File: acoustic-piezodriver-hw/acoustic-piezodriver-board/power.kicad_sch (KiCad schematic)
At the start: 29 parts, among them J2 Conn_02x04_Odd_Even, U1 LM3478MM, U4 LM3478MM, U5 LM3478MM, U8 NCE6005AS

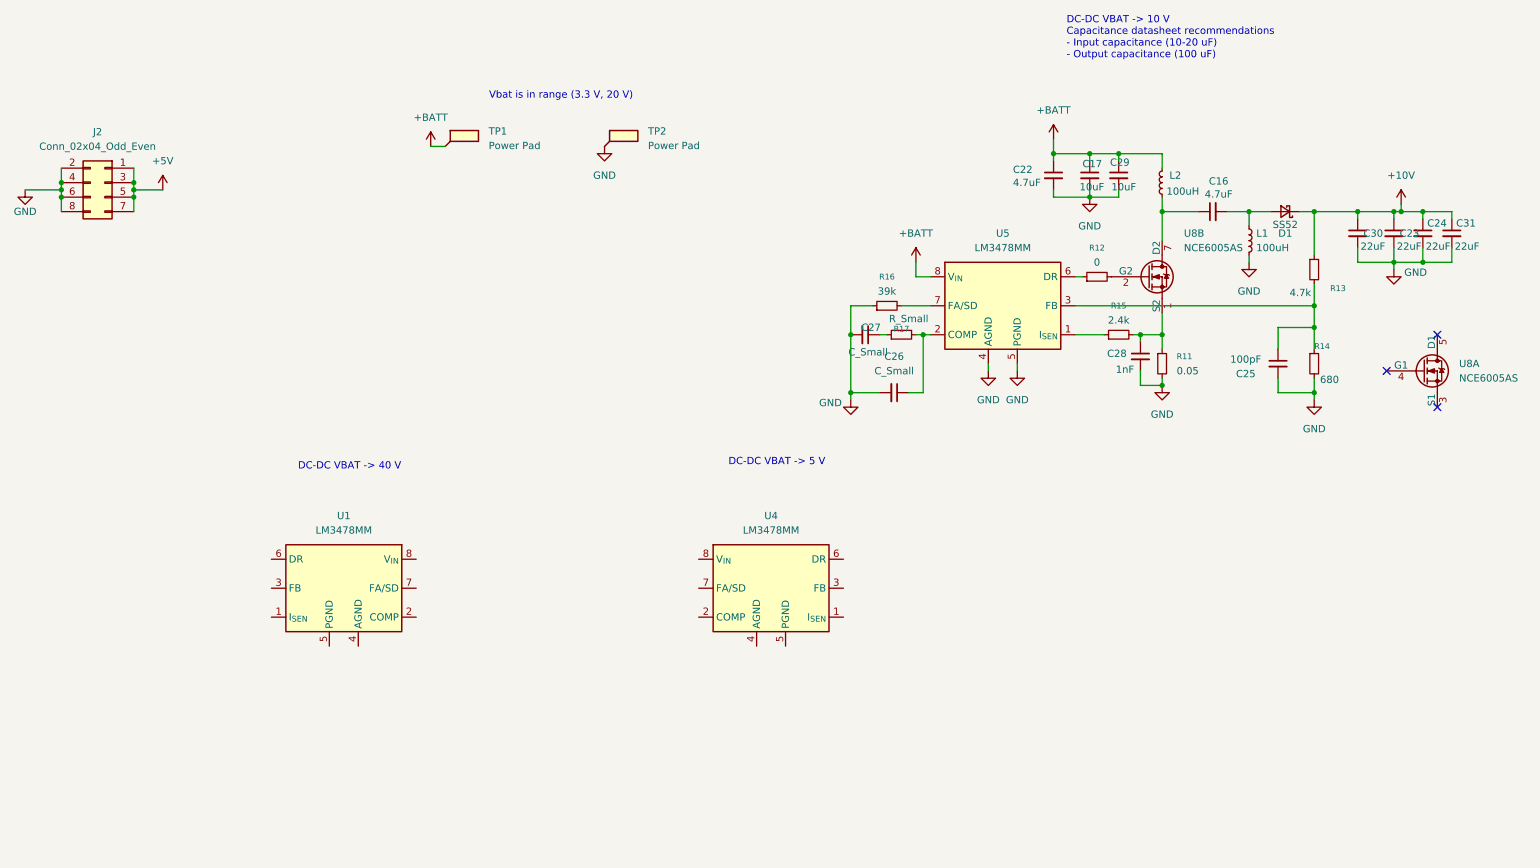
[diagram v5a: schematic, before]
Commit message: [piezodriver] Finished 2 sepic designs, starting boost design (warn) Make sure to max diode voltage difference
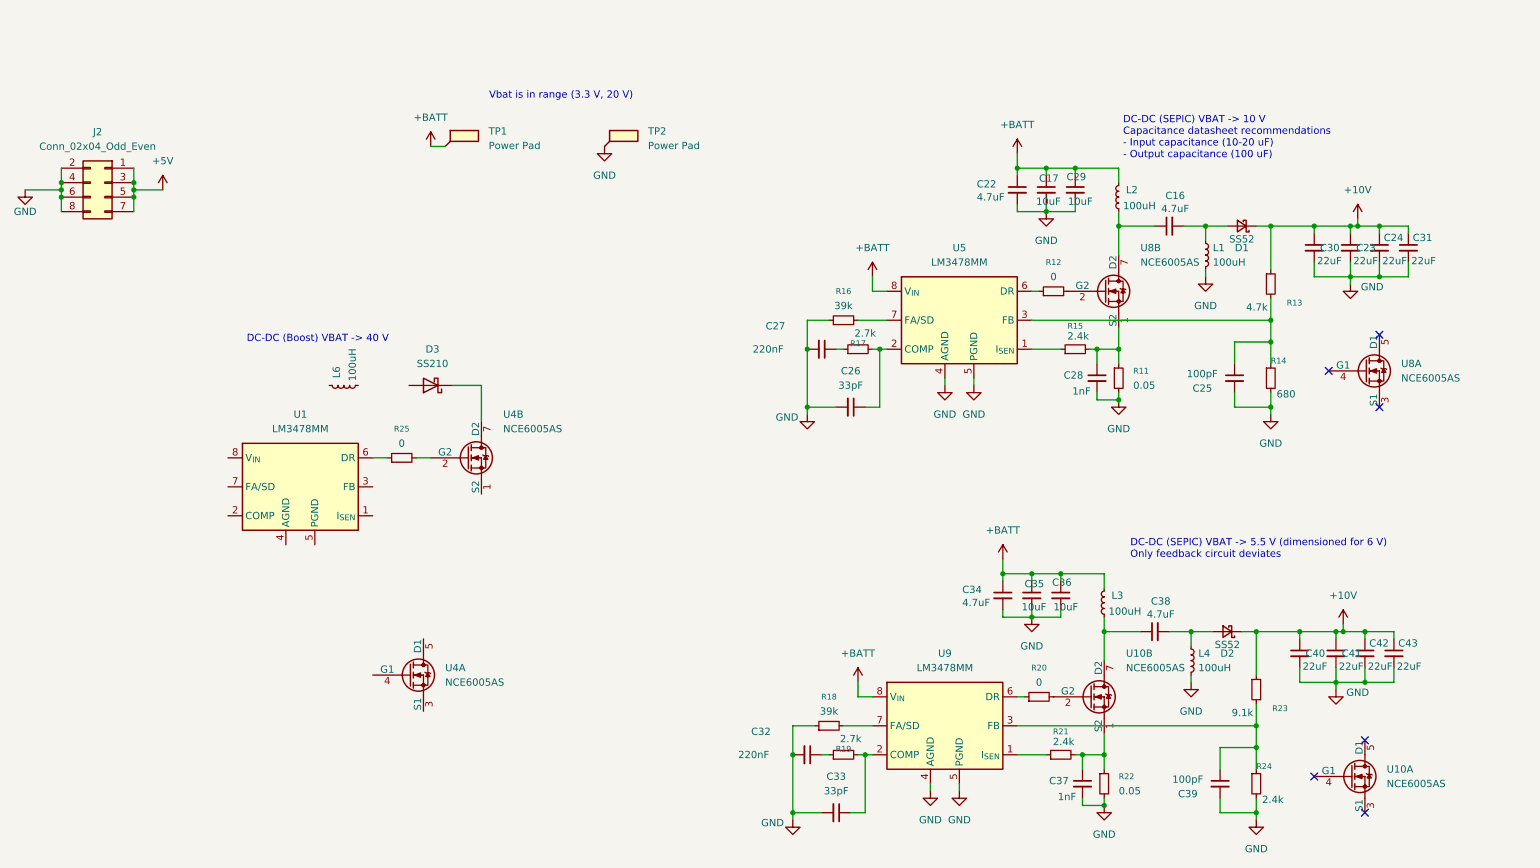
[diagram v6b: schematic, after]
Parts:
- removed U4: LM3478MM, Package_SO:VSSOP-8_3x3mm_P0.65mm, symbol Regulator_Controller:LM3478MM
- added C32: 220nF, Capacitor_SMD:C_0603_1608Metric, symbol Device:C_Small
- added C33: 33pF, Capacitor_SMD:C_0603_1608Metric, symbol Device:C_Small
- added C34, C38: 4.7uF, Capacitor_SMD:C_1206_3216Metric, symbol Device:C_Small
- added C35, C36: 10uF, Capacitor_SMD:C_0805_2012Metric, symbol Device:C_Small
- added C37: 1nF, Capacitor_SMD:C_0402_1005Metric, symbol Device:C_Small
- added C39: 100pF, Capacitor_SMD:C_0402_1005Metric, symbol Device:C_Small
- added C40, C41, C42, C43: 22uF, Capacitor_SMD:C_0805_2012Metric, symbol Device:C_Small
- added D2: SS52, Diode_SMD:D_SMA-SMB_Universal_Handsoldering, symbol Device:D_Schottky_Small
- added D3: SS210, Diode_SMD:D_SMA, symbol Diode:SS210
- added L3, L4, L6: 100uH, symbol Device:L_Small
- added R18: 39k, Resistor_SMD:R_0603_1608Metric, symbol Device:R_Small
- added R19: 2.7k, Resistor_SMD:R_0603_1608Metric, symbol Device:R_Small
- added R20, R25: 0, Resistor_SMD:R_0603_1608Metric_Pad0.98x0.95mm_HandSolder, symbol Device:R_Small
- added R21: 2.4k, Resistor_SMD:R_0805_2012Metric_Pad1.20x1.40mm_HandSolder, symbol Device:R_Small
- added R22: 0.05, Resistor_SMD:R_1206_3216Metric_Pad1.30x1.75mm_HandSolder, symbol Device:R_Small
- added R23: 9.1k, Resistor_SMD:R_0603_1608Metric, symbol Device:R_Small
- added R24: 2.4k, Resistor_SMD:R_0603_1608Metric, symbol Device:R_Small
- added U10, U4: NCE6005AS, symbol custom_mosfet:NCE6005AS
- added U9: LM3478MM, Package_SO:VSSOP-8_3x3mm_P0.65mm, symbol Regulator_Controller:LM3478MM
- C25: footprint (none) -> Capacitor_SMD:C_0402_1005Metric; LPN (none) -> C1546; MPN (none) -> 0402CG101J500NT
- C26: value C_Small -> 33pF; footprint (none) -> Capacitor_SMD:C_0603_1608Metric; LPN (none) -> C1663; MPN (none) -> CL10C330JB8NNNC
- C27: value C_Small -> 220nF; footprint (none) -> Capacitor_SMD:C_0603_1608Metric
- C28: footprint (none) -> Capacitor_SMD:C_0402_1005Metric; LPN (none) -> C1523; MPN (none) -> 0402B102K500NT
- R12: footprint (none) -> Resistor_SMD:R_0603_1608Metric_Pad0.98x0.95mm_HandSolder; LPN (none) -> C15402; MPN (none) -> 0603WAJ0000T5E
- R17: value R_Small -> 2.7k; footprint (none) -> Resistor_SMD:R_0603_1608Metric; LPN (none) -> C13167; MPN (none) -> 0603WAF2701T5E
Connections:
- net +10V: now also C40.1, C41.1, C42.1, C43.1, D2.1 (K), R23.1
- net +BATT: now also C34.1, C35.1, C36.1, L3.2, U9.8 (V_{IN})
- net GND: now also C32.2, C33.2, C34.2, C35.2, C36.2, C37.2, C39.2, C40.2, C41.2, C42.2, C43.2, L4.2, R18.1, R22.2, R24.2, U9.4 (AGND), U9.5 (PGND)
- net at U1.6 (DR): now also R25.1
- new net: U4.5 (D1), U4.6 (D1)
- new net: C38.1, L3.1, U10.7 (D2), U10.8 (D2)
- new net: C38.2, D2.2 (A), L4.1
- new net: R18.2, U9.7 (FA/SD)
- new net: C39.1, R23.2, R24.1, U9.3 (FB)
- new net: C37.1, R21.2, R22.1, U10.1 (S2)
- new net: C32.1, R19.1
- new net: C33.1, R19.2, U9.2 (COMP)
- new net: R25.2, U4.2 (G2)
- new net: D3.1 (K), U4.7 (D2), U4.8 (D2)
- new net: R20.1, U9.6 (DR)
- new net: R20.2, U10.2 (G2)
- new net: R21.1, U9.1 (I_{SEN})
- new net: U10.5 (D1), U10.6 (D1)
- no-connect marks 3 -> 6
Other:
- note added: "DC-DC (Boost) VBAT -> 40 V"
- note added: "DC-DC (SEPIC) VBAT -> 10 V Capacitance datasheet recommendations - Input capacitance (10-20 uF) - Output capacitance (100 uF)"
- note added: "DC-DC (SEPIC) VBAT -> 5.5 V (dimensioned for 6 V) Only feedback circuit deviates"
- note removed: "DC-DC VBAT -> 10 V Capacitance datasheet recommendations - Input capacitance (10-20 uF) - Output capacitance (100 uF)"
- note removed: "DC-DC VBAT -> 40 V"
- note removed: "DC-DC VBAT -> 5 V"
- moved on the sheet: C16, C17, C22, C23, C24, C25, C26, C27, C28, C29, C30, C31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

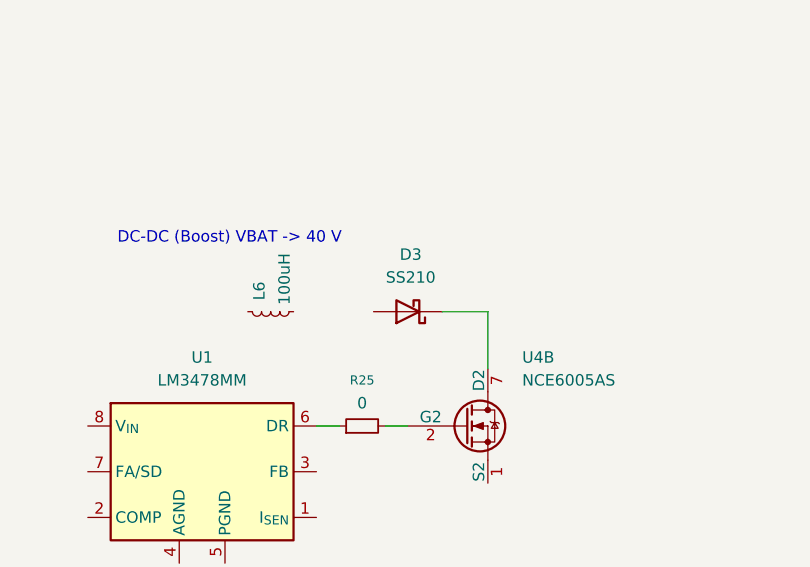
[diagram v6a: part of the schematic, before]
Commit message: [piezodriver] Choose smaller inductor with larger current carrying capacity, increase switching frequency (but check LM3478 limits)
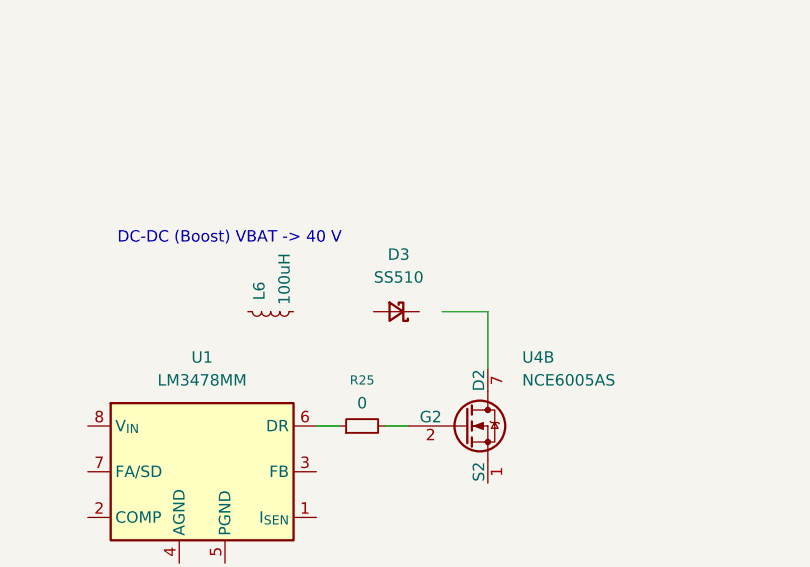
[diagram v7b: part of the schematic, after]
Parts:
- removed D3: SS210, Diode_SMD:D_SMA, symbol Diode:SS210
- added D3: SS510, Diode_SMD:D_SMA, symbol Device:D_Schottky_Small
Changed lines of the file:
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@@
+	)
+	(symbol
+		(lib_id "Device:D_Schottky_Small")
+		(at 97.79 66.04 180)
+		(unit 1)
+		(exclude_from_sim no)
+		(in_bom yes)
+		(on_board yes)
+		(dnp no)
+		(fields_autoplaced yes)
+		(property "Reference" "D3"
+			(at 98.044 59.69 0)
+			(effects
+				(font
+					(size 1.27 1.27)
+				)
+			)
+		)
+		(property "Value" "SS510"
+			(at 98.044 62.23 0)
+			(effects
+				(font
+					(size 1.27 1.27)
+				)
+			)
+		)
+		(property "Footprint" "Diode_SMD:D_SMA"
+			(at 97.79 66.04 90)
+			(effects
+				(font
+					(size 1.27 1.27)
+				)
+				(hide yes)
+			)
+		)
+		(property "Datasheet" "https://jlcpcb.com/api/file/downloadByFileSystemAccessId/8586175771950133248"
+			(at 97.79 66.04 90)
+			(effects
+				(font
+					(size 1.27 1.27)
+				)
+				(hide yes)
+			)
+		)
+		(property "Description" "5A, 100V, Vf 0.85"
+			(at 97.79 66.04 0)
+			(effects
+				(font
+					(size 1.27 1.27)
+				)
+				(hide yes)
+			)
+		)
+		(property "MPN" "SS510"
+			(at 97.79 66.04 0)
+			(effects
+				(font
+					(size 1.27 1.27)
+				)
+				(hide yes)
+			)
+		)
+		(property "LPN" "C65010"
+			(at 97.79 66.04 0)
+			(effects
+				(font
+					(size 1.27 1.27)
+				)
+				(hide yes)
+			)
+		)
+		(pin "2"
+		)
+		(pin "1"
+		)
+		(instances
+			(project ""
+				(path "/94cb090f-214e-44cc-b8ed-ae50ff29d2bf/a0fbc78d-8163-4e6b-8d81-98a3dd6573cb"
+					(reference "D3")
+					(unit 1)
+				)
+			)
+		)
 	)
 	(symbol
@@
 					(unit 1)
 				)
-			)
-		)
-	)
-	(symbol
-		(lib_id "Diode:SS210")
-		(at 99.06 66.04 180)
-		(unit 1)
-		(exclude_from_sim no)
-		(in_bom yes)
-		(on_board yes)
-		(dnp no)
-		(fields_autoplaced yes)
-		(property "Reference" "D3"
-			(at 99.3775 59.69 0)
-			(effects
-				(font
-					(size 1.27 1.27)
-				)
-			)
-		)
-		(property "Value" "SS210"
-			(at 99.3775 62.23 0)
-			(effects
-				(font
-					(size 1.27 1.27)
-				)
-			)
-		)
-		(property "Footprint" "Diode_SMD:D_SMA"
-			(at 99.06 61.595 0)
-			(effects
-				(font
-					(size 1.27 1.27)
-				)
-				(hide yes)
-			)
-		)
-		(property "Datasheet" "https://www.wontop.com/uploadfiles/56/sort_excel/pdf/ss22.pdf"
-			(at 99.06 66.04 0)
-			(effects
-				(font
-					(size 1.27 1.27)
-				)
-				(hide yes)
-			)
-		)
-		(property "Description" "100V, 2A avg"
-			(at 99.06 66.04 0)
-			(effects
-				(font
-					(size 1.27 1.27)
-				)
-				(hide yes)
-			)
-		)
-		(property "LPN" "C14996"
-			(at 99.06 66.04 0)
-			(effects
-				(font
-					(size 1.27 1.27)
-				)
-				(hide yes)
-			)
-		)
-		(property "MPN" "SS210"
-			(at 99.06 66.04 0)
-			(effects
-				(font
-					(size 1.27 1.27)
-				)
-				(hide yes)
-			)
-		)
-		(pin "2"
-		)
-		(pin "1"
-		)
-		(instances
-			(project ""
-				(path "/94cb090f-214e-44cc-b8ed-ae50ff29d2bf/a0fbc78d-8163-4e6b-8d81-98a3dd6573cb"
-					(reference "D3")
-					(unit 1)
-				)

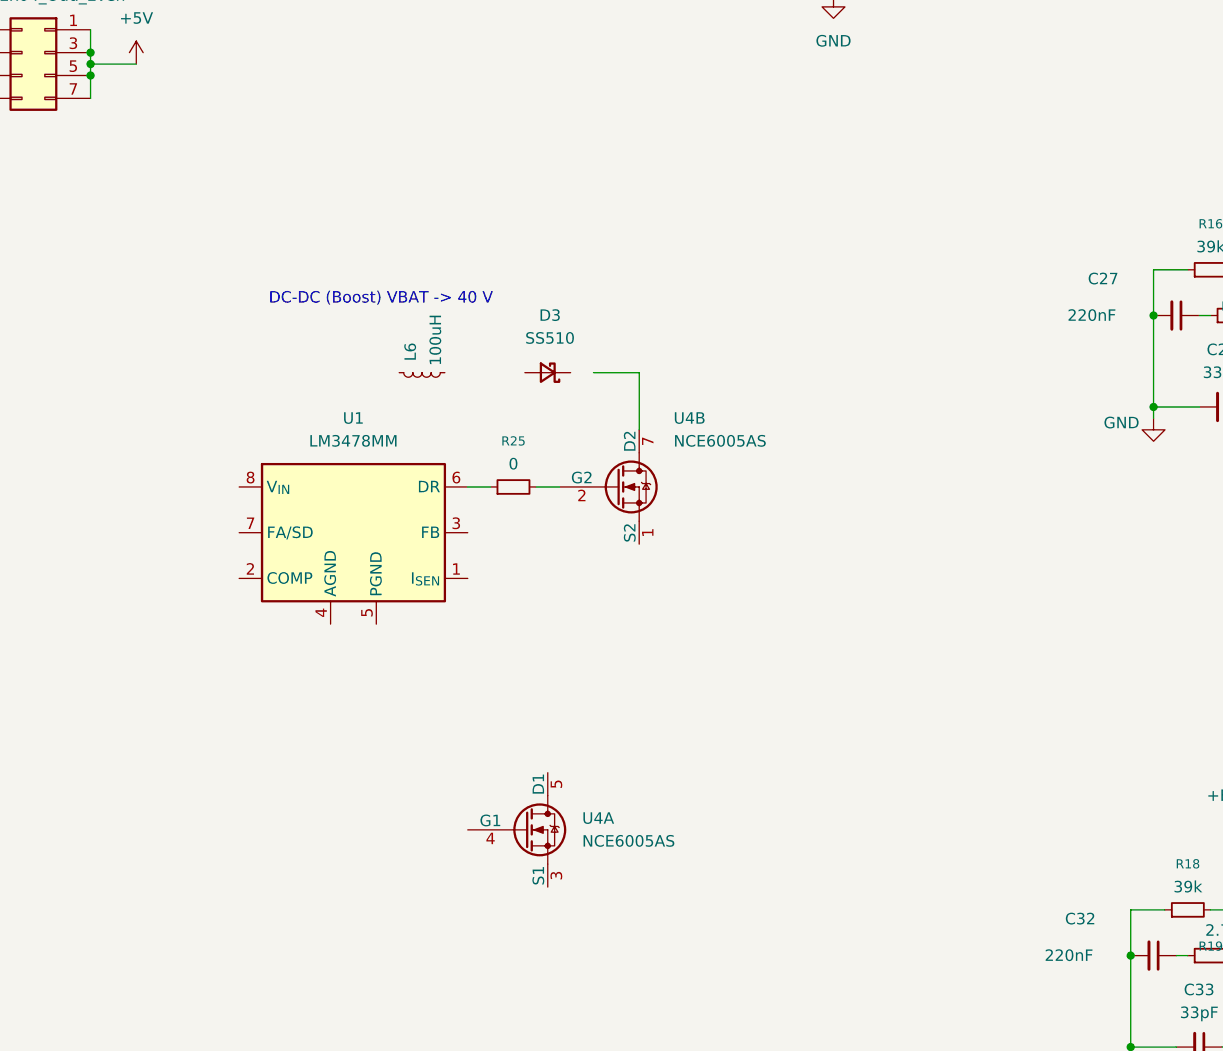
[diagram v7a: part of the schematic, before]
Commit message: [piezodriver] Finished boost converter simulation and part selection, working on compensation circuit and control loop
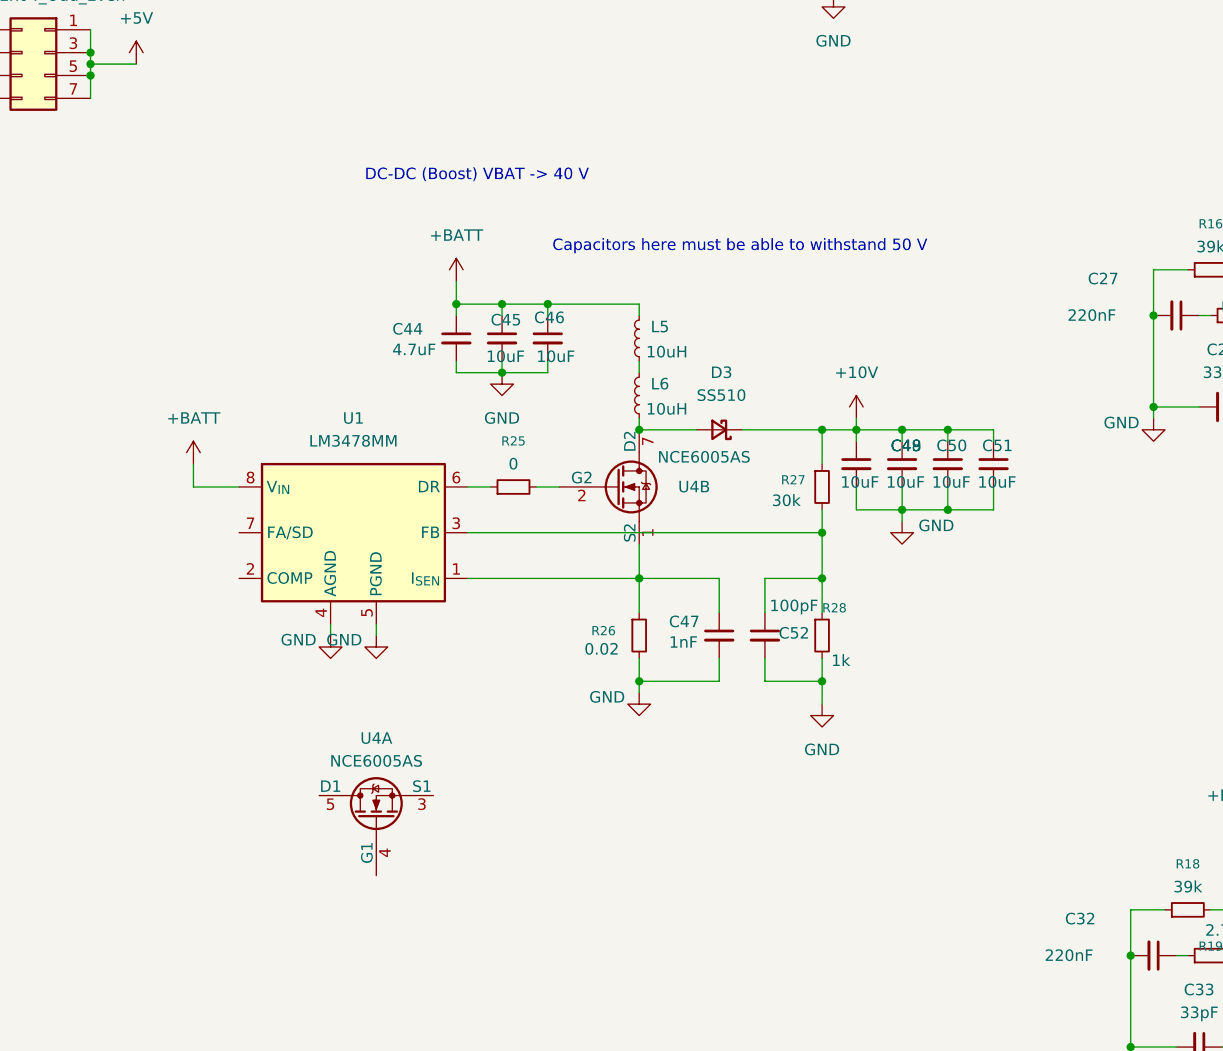
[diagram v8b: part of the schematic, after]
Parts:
- added C44: 4.7uF, Capacitor_SMD:C_1206_3216Metric, symbol Device:C_Small
- added C45, C46, C48, C49, C50, C51: 10uF, Capacitor_SMD:C_0805_2012Metric, symbol Device:C_Small
- added C47: 1nF, Capacitor_SMD:C_0402_1005Metric, symbol Device:C_Small
- added C52: 100pF, Capacitor_SMD:C_0402_1005Metric, symbol Device:C_Small
- added L5: 10uH, symbol Device:L_Small
- added R26: 0.02, Resistor_SMD:R_1206_3216Metric_Pad1.30x1.75mm_HandSolder, symbol Device:R_Small
- added R27: 30k, Resistor_SMD:R_0603_1608Metric, symbol Device:R_Small
- added R28: 1k, Resistor_SMD:R_0603_1608Metric, symbol Device:R_Small
- L6: value 100uH -> 10uH; LPN C436577 -> C475915; MPN PSPMAC1045H-101M-ANP -> FXL1040-100-M
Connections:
- net +10V: now also D3.1 (K), C48.1, C49.1, C50.1, C51.1, R27.1
- net +BATT: now also U1.8 (V_{IN}), C44.1, C45.1, C46.1, L5.2
- net GND: now also U1.4 (AGND), U1.5 (PGND), C44.2, C45.2, C46.2, C47.2, C48.2, C49.2, C50.2, C51.2, C52.2, R26.2, R28.2
- net at D3.2 (A): now also L6.1, U4.7 (D2), U4.8 (D2)
- net at U4.1 (S2): now also U1.1 (I_{SEN}), C47.1, R26.1
- net at U1.3 (FB): now also C52.1, R27.2, R28.1
- net at L6.2: now also L5.1
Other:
- note added: "Capacitors here must be able to withstand 50 V"
- moved on the sheet: D3, U4A
